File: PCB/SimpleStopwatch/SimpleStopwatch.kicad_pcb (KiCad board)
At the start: 2 copper layers, 85 x 30 mm, 30 parts, among them J1 Switch, J2 Power, U1 L7805, U2 ATmega328P-AU, U3 ULN2003, Y1 Crystal_Small

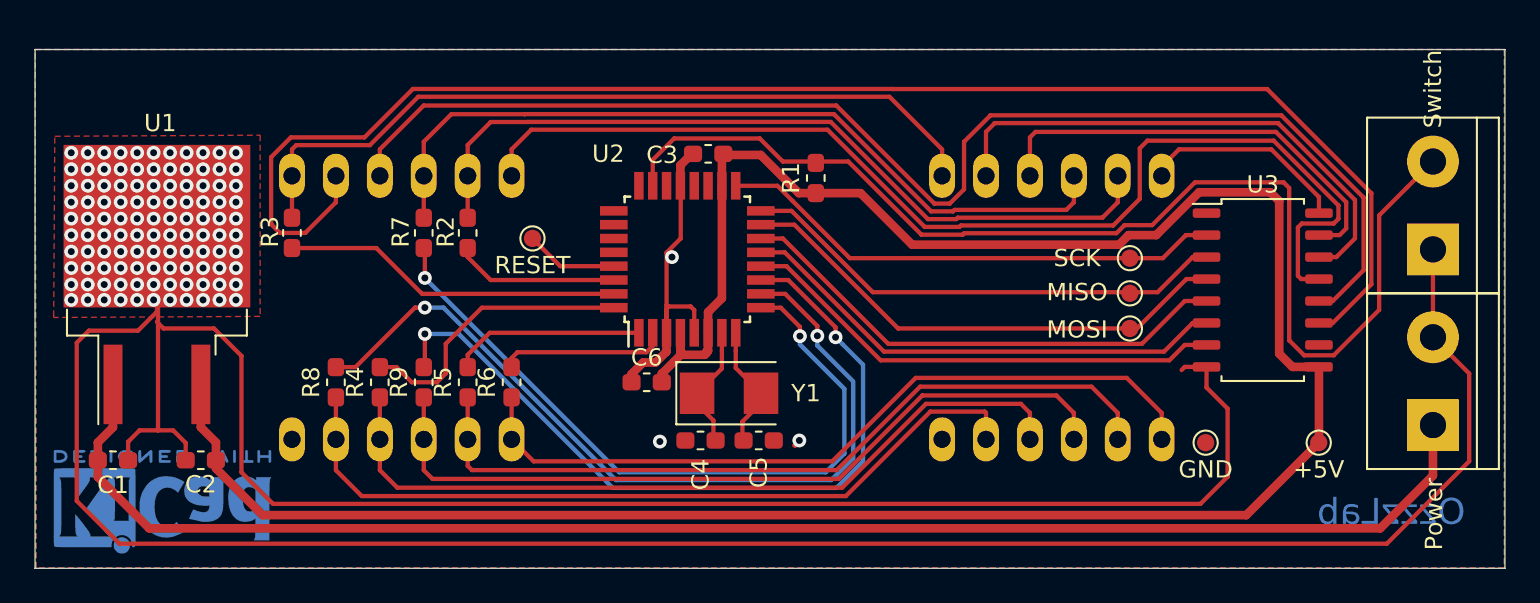
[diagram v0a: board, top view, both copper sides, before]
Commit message: Removed ULN2003 Mistake
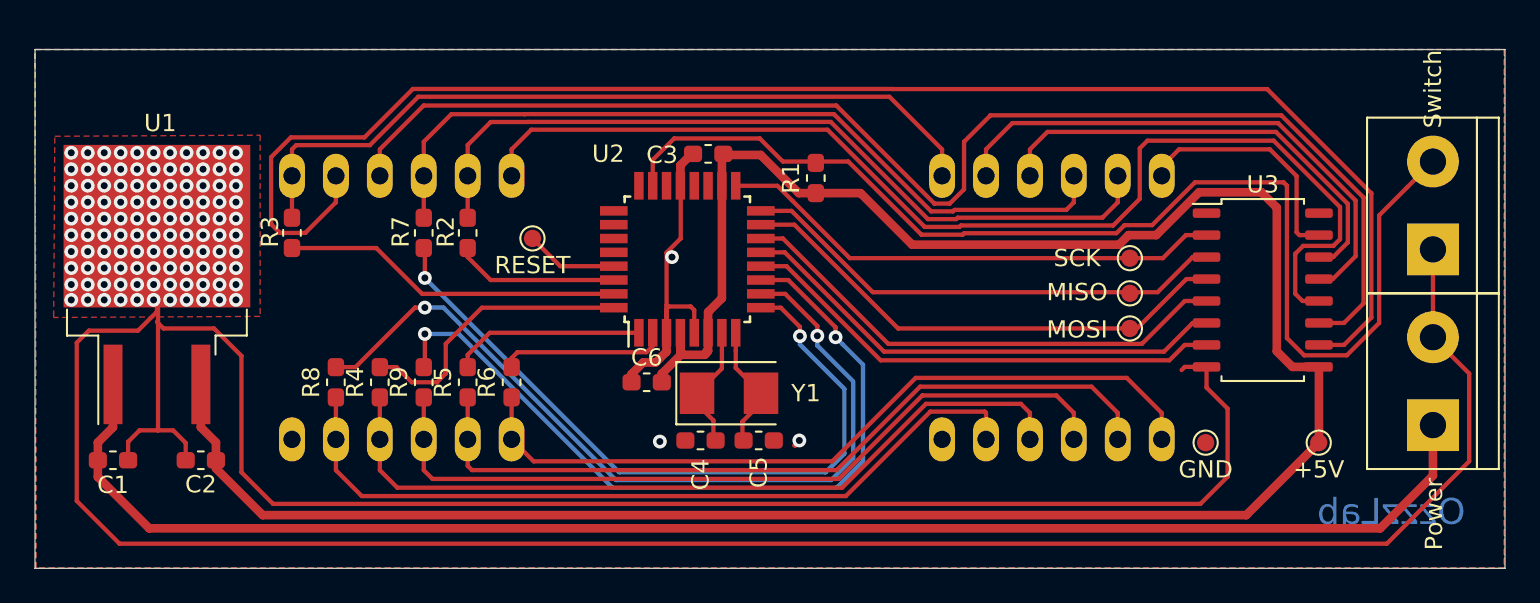
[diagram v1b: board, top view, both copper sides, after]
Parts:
- removed REF**: KiCad-Logo2_5mm_Copper, Symbol:KiCad-Logo2_5mm_Copper
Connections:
- U3 pad 10: (no net) -> Net-(LED2-PadDIG3)
- U3 pad 11: Net-(LED2-PadDIG3) -> Net-(LED2-PadDIG2)
- U3 pad 12: Net-(LED2-PadDIG2) -> Net-(LED2-PadDIG1)
- U3 pad 13: Net-(LED2-PadDIG1) -> Net-(LED1-PadDIG3)
- U3 pad 14: Net-(LED1-PadDIG3) -> Net-(LED1-PadDIG2)
- U3 pad 15: Net-(LED1-PadDIG2) -> Net-(LED1-PadDIG1)
- U3 pad 16: Net-(LED1-PadDIG1) -> (no net)
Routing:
- net Net-(LED1-PadDIG1): track 12.1 -> 14.0 mm
- net Net-(LED2-PadDIG2): track 75.0 -> 76.7 mm
- net Net-(LED2-PadDIG3): track 87.2 -> 88.9 mm
- net Net-(LED2-PadDIG1): track 64.9 -> 66.3 mm
- net Net-(LED1-PadDIG2): track 25.6 -> 26.3 mm
- net Net-(LED1-PadDIG3): track 30.7 -> 31.3 mm

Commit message: Changed LDO to DCDC module board
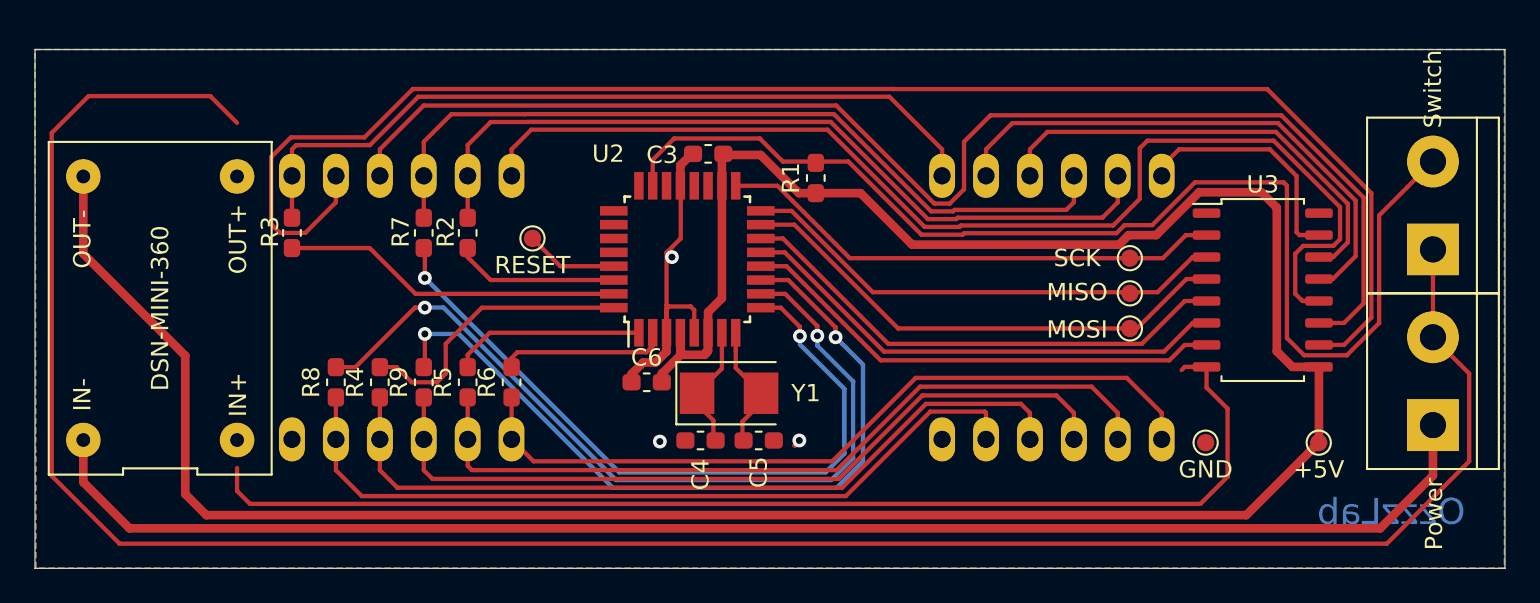
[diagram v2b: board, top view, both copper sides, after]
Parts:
- removed C1, C2: 0.1u, Capacitor_SMD:C_0603_1608Metric_Pad1.05x0.95mm_HandSolder
- removed U1: L7805, Package_TO_SOT_SMD:TO-263-2
- added PS1: DSN-MINI-360, !MyFootprints:Mini360, F.Cu at (7.24, 15.0)
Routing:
- net +5V: track 141.1 -> 157.8 mm
- net GND: track 233.2 -> 218.8 mm, vias 113 -> 3
- net +24V: track 88.3 -> 85.8 mm

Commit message: Some PCB improvements
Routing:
- net GND: track 218.8 -> 219.5 mm

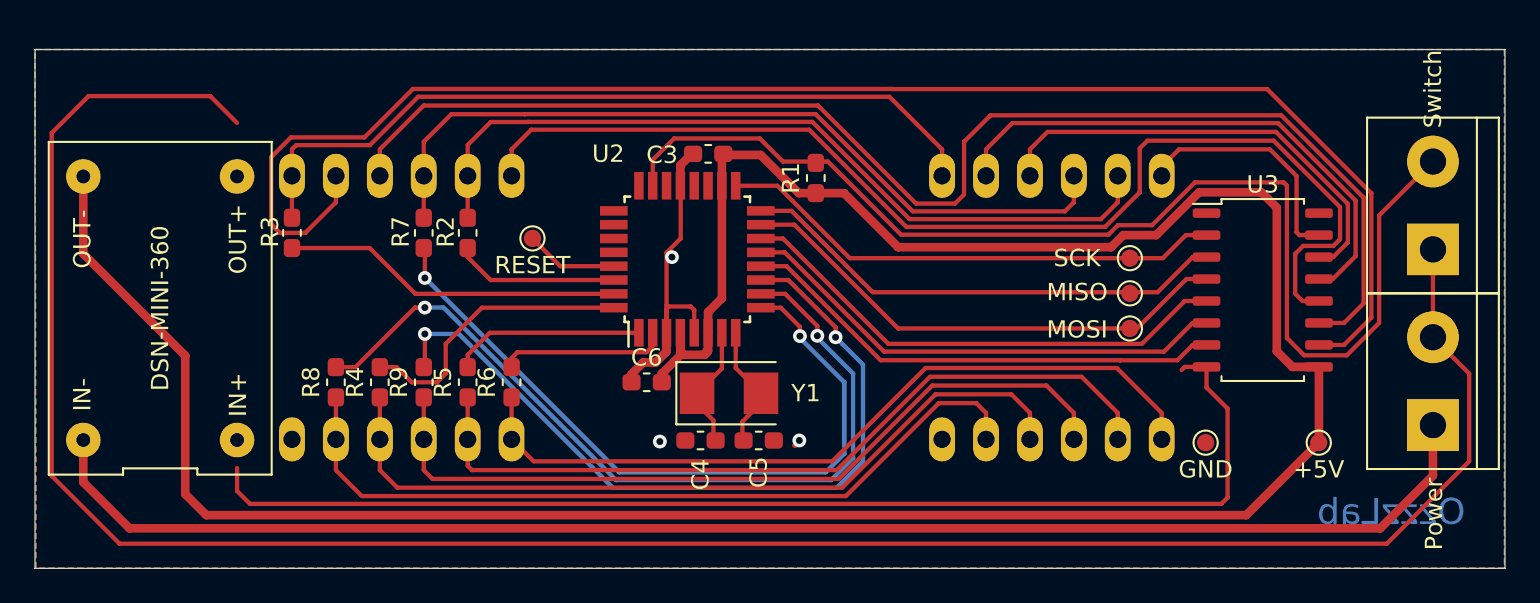
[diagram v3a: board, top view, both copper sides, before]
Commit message: Added TPS5430 DCDC. Yuri version
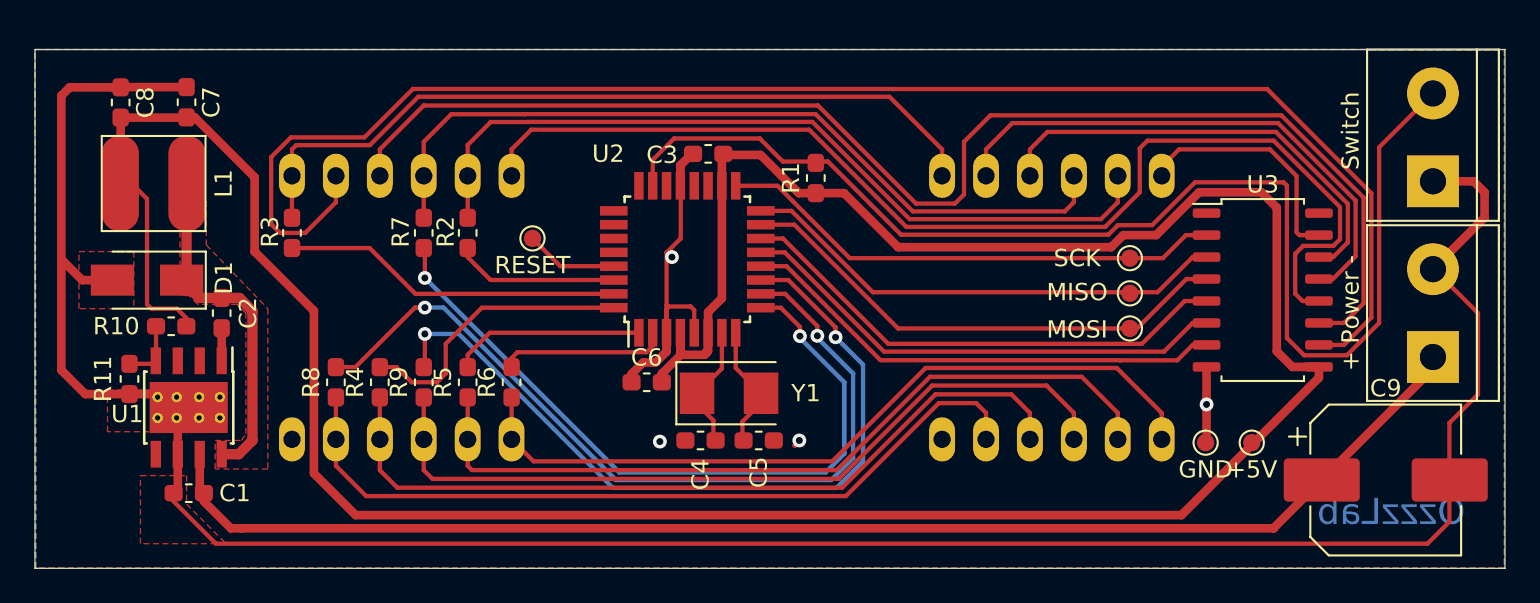
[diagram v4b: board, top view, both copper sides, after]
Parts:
- removed PS1: DSN-MINI-360, !MyFootprints:Mini360
- added C1: 22u, Capacitor_SMD:C_0603_1608Metric_Pad1.05x0.95mm_HandSolder, F.Cu at (8.89, 25.7)
- added C2: 0.1u, Capacitor_SMD:C_0603_1608Metric_Pad1.05x0.95mm_HandSolder, F.Cu at (10.8, 15.2)
- added C7: 22u, Capacitor_SMD:C_0603_1608Metric_Pad1.05x0.95mm_HandSolder, F.Cu at (8.76, 3.05)
- added C8: 22u, Capacitor_SMD:C_0603_1608Metric_Pad1.05x0.95mm_HandSolder, F.Cu at (4.95, 3.06)
- added C9: 100uF, Capacitor_SMD:CP_Elec_8x10.5, F.Cu at (78.1, 24.9)
- added D1: B120-E3, Diode_SMD:D_SMA, F.Cu at (6.48, 13.3)
- added L1: L_Small, !MyFootprints:Inductor_CD54_Sumida, F.Cu at (6.86, 7.75)
- added R10: 1k, Resistor_SMD:R_0603_1608Metric_Pad1.05x0.95mm_HandSolder, F.Cu at (7.87, 16.0)
- added R11: 1k, Resistor_SMD:R_0603_1608Metric_Pad1.05x0.95mm_HandSolder, F.Cu at (5.46, 19.1)
- added U1: TPS5430DDA, Package_SO:TI_SO-PowerPAD-8_ThermalVias, F.Cu at (8.89, 20.7)
- J2: value Power -> + Power -
- LED1, LED2: footprint !MyFootprints:BC56-12SRWA -> !MyFootprints:LED_7SEG_3DIG_CC_0.56
- moved J1 3.94 mm to (80.8, 7.62)
- moved J2 3.94 mm to (80.8, 17.8)
- moved H5 3.87 mm to (70.4, 22.7)
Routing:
- net GND: track 219.5 -> 164.2 mm, vias 3 -> 4
- net Net-(C2-Pad1): track 0.00 -> 19.9 mm
- net +5V: track 158.0 -> 170.7 mm
- net +24V: track 85.8 -> 79.1 mm
- net SW: track 68.3 -> 72.2 mm
- net Net-(R10-Pad1): track 0.00 -> 3.60 mm
- net Net-(C2-Pad2): track 0.00 -> 1.89 mm
- added copper zone on F.Cu, net Net-(C2-Pad1)
